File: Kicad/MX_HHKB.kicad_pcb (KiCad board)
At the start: 2 copper layers, 285.8 x 95.2 mm, 143 parts, among them J1 USB_mini_micro_B, K1 Esc, K10 9, K11 0, K12 -, K13 =, K14 Tab, K15 Q, K16 W, K17 E, K18 R, K19 T, K2 1, K20 Y, K21 U, K22 I, K23 O, K24 P, K25 [, K26 ], K27 Ctrl, K28 A, K29 S, K3 2, K30 D, K31 F, K32 G, K33 H, K34 J, K35 K, K36 L, K37 ;, K38 ', K39 Enter, K4 3, K40 L_Shift, K41 Z, K42 X, K43 C, K44 V, K45 B, K46 N, K47 M, K48 ,, K49 ., K5 4, K50 /, K51 R_Shift, K52 Fn, K53 L_GUI, K54 L_ALT, K55 SPACE, K56 R_ALT, K57 R_GUI, K58 `, K59 \, K6 5, K60 BACKSPACE, K61 Ctrl, K7 6, K8 7, K9 8, SW1 SW_PUSH, U0 ATMEGA32U4, X1 XTAL_GND

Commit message: - Added darkou and open hardware logo - Updated col/row assignation (simplifying rooting)
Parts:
- added G***: LOGO, Footprint:OPEN-HARDWARE, B.Cu at (192.2, 181.2)
- added G***: LOGO, Footprint:darkou, B.Cu at (236.8, 182.0)
- added G***: LOGO, Footprint:darkou, F.Cu at (234.5, 181.8)
- moved D14 10.5 mm to (96.2, 132.8), turned to 180 degrees
- moved R1 5.00 mm to (92.2, 152.5)
- moved C8 4.45 mm to (92.8, 171.2), turned to 0 degrees
- moved X1 3.82 mm to (96.0, 184.8)
- moved D1 3.01 mm to (82.5, 115.0)
- moved R3 2.30 mm to (72.0, 120.2)
- moved Poker_side_edge_long 0.91 mm to (352.2, 153.8)
- moved Poker_side_edge_long 0.66 mm to (66.8, 153.8)
- moved C1 0.35 mm to (91.5, 189.0), turned to 225 degrees
- turned SW1 to 90 degrees
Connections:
- U0 pad 11: /Col3 -> /Col1
- U0 pad 21: /Row0 -> /Col9
- U0 pad 22: /Row2 -> /Col4
- U0 pad 25: /Row1 -> /Col5
- U0 pad 28: /Col4 -> /Row1
- U0 pad 29: /Col5 -> /Row2
- U0 pad 31: /Col8 -> /Row0
- U0 pad 32: /Col9 -> /Col8
- U0 pad 9: /Col1 -> /Col3
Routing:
- net /Row3: track 266.9 -> 285.9 mm, vias 3 -> 2
- net VCC: track 171.3 -> 153.5 mm, vias 4 -> 2
- net GND: track 248.2 -> 262.9 mm, vias 0 -> 2
- net /Row4: track 364.7 -> 350.2 mm, vias 3 -> 1
- net /Col4: track 192.8 -> 179.1 mm, vias 3 -> 2
- net /Row1: track 323.8 -> 311.6 mm, vias 1 -> 2
- net /Row2: track 371.4 -> 359.4 mm
- net Net-(R1-Pad2): track 60.6 -> 51.1 mm, vias 2 -> 5
- net /Col5: track 235.8 -> 227.3 mm, vias 4 -> 2
- net Net-(D14-Pad2): track 9.39 -> 15.6 mm
- net Net-(C8-Pad1): track 12.5 -> 6.63 mm
- net Net-(C1-Pad1): track 18.5 -> 13.8 mm
- net Net-(J1-Pad2): track 27.0 -> 31.7 mm
- net /Col8: track 301.6 -> 296.9 mm, vias 7 -> 3
- net /Col12: track 360.7 -> 356.1 mm
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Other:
- board text added: "DK60 rev.A"

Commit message: - Rerouting some wires - Added led on Esc and Caps locks switches
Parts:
- added LD0: ESC_LED, LEDs:LED_D3.0mm, F.Cu at (75.0, 111.8)
- added LD1: CAPS_LED, LEDs:LED_D3.0mm, F.Cu at (77.2, 149.8)
- added LD2: CAPS_LED, LEDs:LED_D3.0mm, F.Cu at (84.8, 149.8)
- added R5: R, Resistors_SMD:R_0805_HandSoldering, B.Cu at (76.2, 116.0)
- added R6: R, Resistors_SMD:R_0805_HandSoldering, B.Cu at (84.0, 157.0)
- X1: footprint Crystals:Crystal_SMD_SeikoEpson_TSX3225-4pin_3.2x2.5mm_HandSoldering -> Footprint:FA-238
- moved R3 52.0 mm to (106.8, 159.0), turned to 45 degrees
- moved R4 50.0 mm to (109.5, 161.0), turned to 225 degrees
- moved C2 11.1 mm to (92.2, 186.0)
- moved C1 10.8 mm to (99.8, 182.0), turned to 315 degrees
- moved C8 2.26 mm to (90.5, 171.0)
- moved D1 1.90 mm to (84.2, 115.8), turned to 180 degrees
- moved R2 1.77 mm to (77.8, 167.5), turned to 135 degrees
- moved D54 1.27 mm to (143.0, 184.5)
- moved X1 1.03 mm to (97.0, 185.0), turned to 315 degrees
- moved C6 1.00 mm to (77.8, 162.5)
- moved C7 1.00 mm to (71.8, 164.8)
- moved C4 0.79 mm to (77.5, 158.0), turned to 225 degrees
- moved D53 0.75 mm to (119.0, 185.0)
- moved C5 0.50 mm to (71.8, 161.0)
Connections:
- U0 pad 15: Net-(U0-Pad15) -> GND
- U0 pad 23: Net-(U0-Pad23) -> GND
- U0 pad 28: /Row1 -> /Row2
- U0 pad 29: /Row2 -> /Row1
- U0 pad 40: Net-(U0-Pad40) -> /CAPS_LED
- U0 pad 41: Net-(U0-Pad41) -> /ESC_LED
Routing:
- net /Row0: track 458.2 -> 656.6 mm, vias 4 -> 3
- net /Row1: track 311.6 -> 405.6 mm, vias 2 -> 3
- net /ESC_LED: track 0.00 -> 63.0 mm, vias 0 -> 2
- net Net-(J1-Pad3): track 31.7 -> 84.2 mm, vias 0 -> 2
- net Net-(J1-Pad2): track 31.7 -> 84.1 mm, vias 0 -> 2
- net /Row2: track 359.4 -> 397.1 mm, vias 1 -> 3
- net Net-(R3-Pad1): track 58.7 -> 28.6 mm
- net Net-(R1-Pad2): track 51.1 -> 75.5 mm, vias 5 -> 4
- net Net-(R4-Pad2): track 53.3 -> 29.7 mm, vias 0 -> 2
- net /CAPS_LED: track 0.00 -> 21.3 mm, vias 0 -> 2
- net /Row3: track 285.9 -> 266.9 mm
- net GND: track 262.9 -> 246.7 mm, vias 2 -> 9
- net Net-(D27-Pad2): track 34.6 -> 23.4 mm
- net Net-(LD1-Pad2): track 0.00 -> 9.56 mm
- net /Col0: track 83.9 -> 90.8 mm
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
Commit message: - Some routing updates
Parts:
- moved R2 3.05 mm to (76.0, 170.0), turned to 90 degrees
- moved R3 1.06 mm to (106.0, 158.2)
- moved R4 1.03 mm to (109.8, 162.0)
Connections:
- U0 pad 1: Net-(U0-Pad1) -> /CAPS_LED
- U0 pad 21: /Col9 -> /Col4
- U0 pad 22: /Col4 -> /Col5
- U0 pad 25: /Col5 -> /Row4
- U0 pad 27: /Row4 -> /Row2
- U0 pad 28: /Row2 -> /Row1
- U0 pad 29: /Row1 -> /Col6
- U0 pad 30: /Col6 -> /Row0
- U0 pad 31: /Row0 -> /Col8
- U0 pad 32: /Col8 -> /Col9
- U0 pad 40: /CAPS_LED -> Net-(U0-Pad40)
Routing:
- net /Row2: track 397.1 -> 491.6 mm, vias 3 -> 0
- net GND: track 246.7 -> 321.7 mm, vias 9 -> 4
- net /Row1: track 405.6 -> 455.3 mm, vias 3 -> 0
- net /Col9: track 331.7 -> 369.9 mm, vias 1 -> 0
- net /Row0: track 656.6 -> 680.9 mm, vias 3 -> 1
- net /ESC_LED: track 63.0 -> 74.6 mm, vias 2 -> 0
- net /Col2: track 142.9 -> 132.3 mm, vias 3 -> 1
- net Net-(R1-Pad2): track 75.5 -> 65.2 mm, vias 4 -> 2
- net /Col5: track 226.2 -> 218.1 mm
- net /CAPS_LED: track 21.3 -> 13.9 mm, vias 2 -> 0
- net /Col8: track 302.0 -> 307.3 mm
- net Net-(R4-Pad2): track 29.7 -> 34.9 mm, vias 2 -> 0
- net Net-(J1-Pad3): track 84.2 -> 88.8 mm
- net /Col0: track 90.8 -> 86.3 mm
- net Net-(R2-Pad1): track 14.3 -> 9.86 mm
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
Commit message: - Cleaning routing, again and again
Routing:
- net /Row0: track 680.9 -> 572.9 mm, vias 1 -> 2
- net GND: track 321.7 -> 293.3 mm, vias 4 -> 1
- net /Row2: track 491.6 -> 480.6 mm
- net /Col8: track 307.3 -> 314.3 mm
- net Net-(J1-Pad2): track 82.5 -> 87.6 mm, vias 2 -> 0
- net /ESC_LED: track 74.6 -> 77.1 mm
- net Net-(J1-Pad3): track 88.8 -> 89.9 mm, vias 2 -> 0
- net Net-(R1-Pad2): track 65.2 -> 66.3 mm
- net /Col3: track 143.6 -> 142.8 mm

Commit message: - Updated layout to allow choice in 3 combinations for bottom row
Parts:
- removed K61: Ctrl, Footprint:Mx_Alps_175_STEPPED
- added K271: Ctrl, Footprint:Mx_Alps_175_STEPPED, F.Cu at (78.6, 145.3)
- added K541: L_ALT, Footprint:Mx_Alps_125, F.Cu at (131.0, 183.4)
- added K551: SPACE, Footprint:Mx_Alps_600, F.Cu at (214.3, 183.4)
- added K552: SPACE, Footprint:Mx_Alps_700, F.Cu at (209.6, 183.4)
- added K561: R_ALT, Footprint:Mx_Alps_150, F.Cu at (276.2, 183.4)
- added K562: R_ALT, Footprint:Mx_Alps_125, F.Cu at (288.1, 183.4)
- added K571: R_GUI, Footprint:Mx_Alps_100, F.Cu at (300.0, 183.4)
- added K572: R_GUI, Footprint:Mx_Alps_100, F.Cu at (309.6, 183.4)
- moved D56 25.4 mm to (264.9, 186.3)
- moved D55 8.50 mm to (224.8, 186.0)
- moved D57 7.85 mm to (321.3, 182.2)
- moved G*** 6.39 mm to (239.8, 178.2)
- moved G*** 3.87 mm to (238.4, 178.5)
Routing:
- net Net-(D56-Pad2): track 8.10 -> 32.9 mm
- net Net-(D57-Pad2): track 8.36 -> 28.8 mm
- net /Col9: track 369.9 -> 388.0 mm
- net /Row2: track 480.6 -> 498.5 mm
- net /Col8: track 314.3 -> 331.6 mm
- net /Row1: track 455.7 -> 469.2 mm
- net /Col5: track 218.1 -> 231.5 mm
- net /Col6: track 253.7 -> 266.0 mm
- net Net-(D55-Pad2): track 7.92 -> 16.7 mm
- net (no net): track 3.30 -> 10.7 mm
- net /Row0: track 572.9 -> 577.4 mm
- net Net-(D54-Pad2): track 7.97 -> 10.4 mm
- net /Col2: track 132.3 -> 134.7 mm
- net /Row4: track 348.3 -> 350.0 mm
- net /Col4: track 177.1 -> 178.4 mm
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
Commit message: - Updated bottom row
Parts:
- moved C1 4.31 mm to (96.3, 179.3), turned to 180 degrees
- moved X1 1.47 mm to (95.5, 185.2)
- moved C2 1.07 mm to (91.3, 185.6)
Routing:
- net Net-(D53-Pad2): track 7.99 -> 31.5 mm
- net /Col1: track 109.6 -> 118.7 mm
- net Net-(C2-Pad1): track 13.2 -> 11.6 mm
- net GND: track 293.3 -> 292.3 mm
- net /Col5: track 231.5 -> 232.1 mm

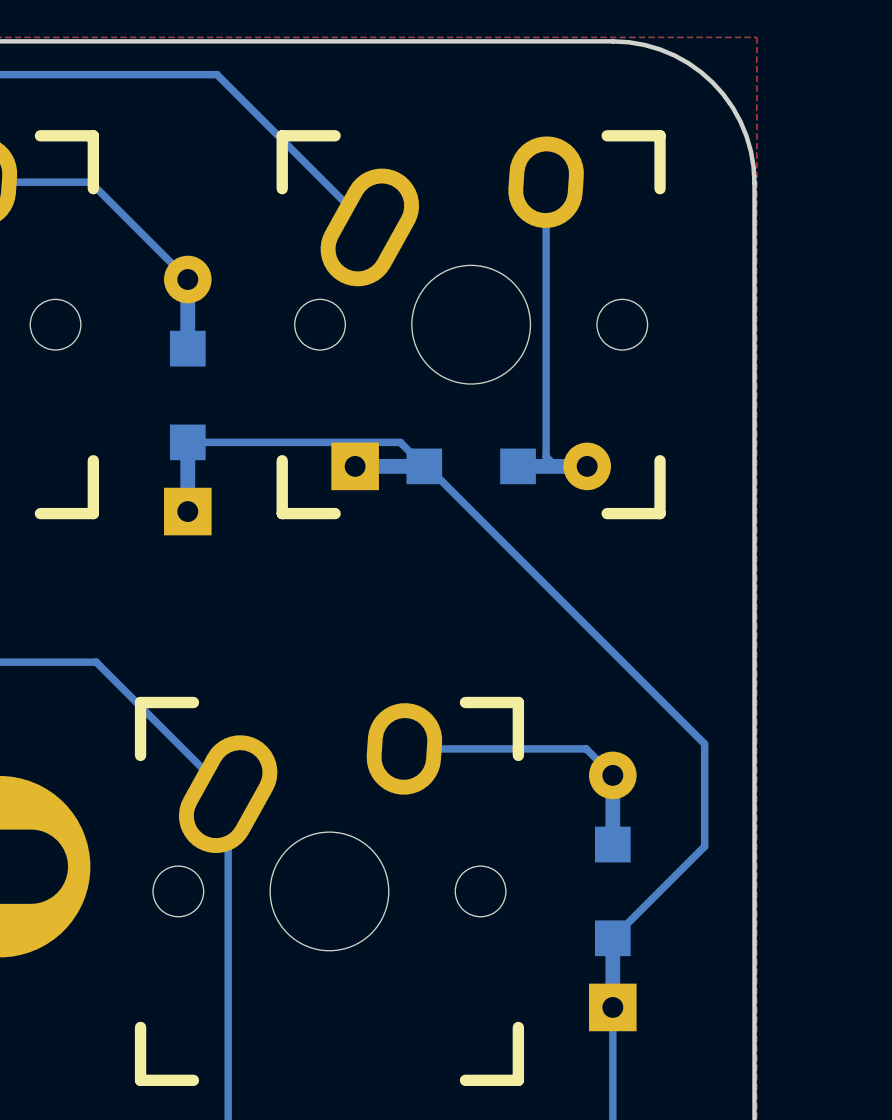
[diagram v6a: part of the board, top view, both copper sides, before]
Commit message: - Updated switches label (K00 to K4C) - Fixed footprint - Updated gerber files
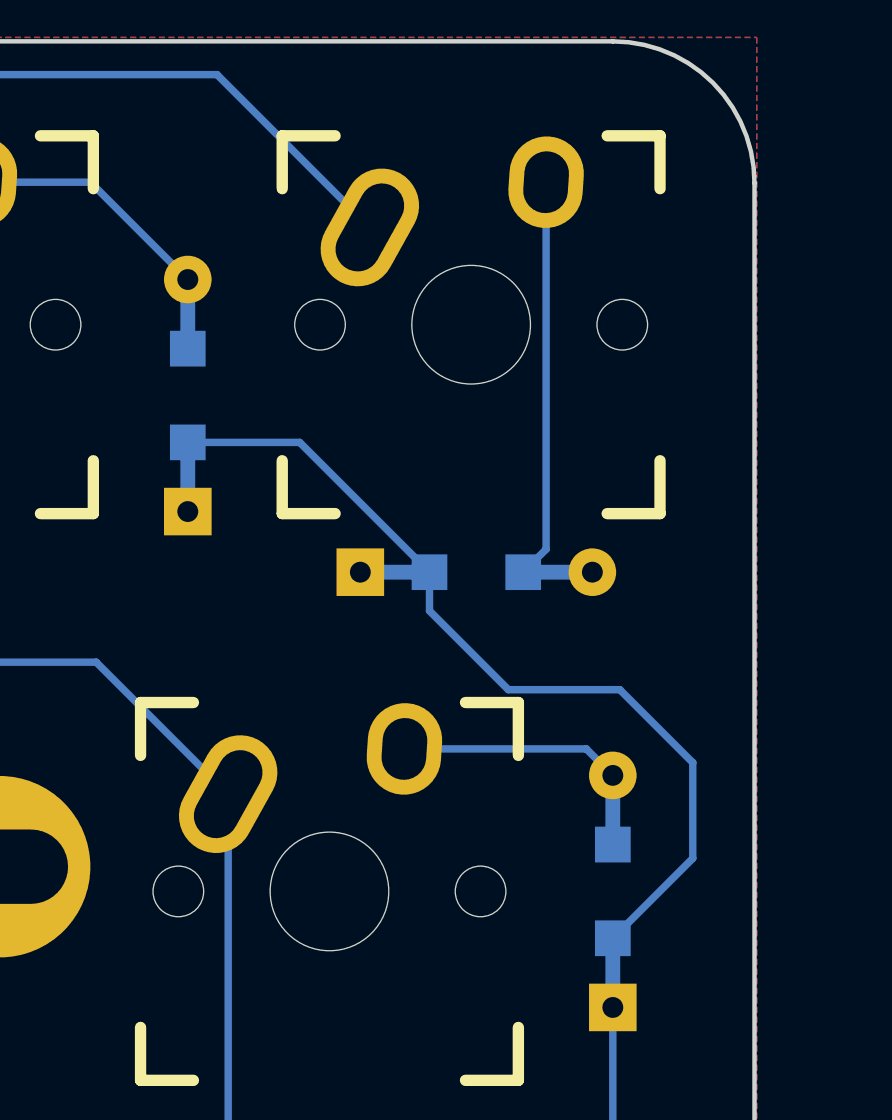
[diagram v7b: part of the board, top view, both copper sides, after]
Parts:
- removed K271: Ctrl, Footprint:Mx_Alps_175_STEPPED
- removed K541: L_ALT, Footprint:Mx_Alps_125
- removed K551: SPACE, Footprint:Mx_Alps_600
- removed K552: SPACE, Footprint:Mx_Alps_700
- removed K561: R_ALT, Footprint:Mx_Alps_150
- removed K562: R_ALT, Footprint:Mx_Alps_125
- removed K571, K572: R_GUI, Footprint:Mx_Alps_100
- added K61: Ctrl, Footprint:Mx_Alps_175_STEPPED, F.Cu at (78.6, 145.3)
- added K62: L_ALT, Footprint:Mx_Alps_125, F.Cu at (131.0, 183.4)
- added K63: SPACE, Footprint:Mx_Alps_700, F.Cu at (209.6, 183.4)
- added K64: SPACE, Footprint:Mx_Alps_600, F.Cu at (214.3, 183.4)
- added K65: R_ALT, Footprint:Mx_Alps_125, F.Cu at (288.1, 183.4)
- added K66: R_ALT, Footprint:Mx_Alps_150, F.Cu at (276.2, 183.4)
- added K67: R_GUI, Footprint:Mx_Alps_100, F.Cu at (309.6, 183.4)
- added K68: R_GUI, Footprint:Mx_Alps_100, F.Cu at (300.0, 183.4)
- K1: value Esc -> K00; footprint Fooprints:Mx_Alps_100 -> Footprint:Mx_Alps_100
- K10: value 9 -> K09; footprint Fooprints:Mx_Alps_100 -> Footprint:Mx_Alps_100
- K11: value 0 -> K0A; footprint Fooprints:Mx_Alps_100 -> Footprint:Mx_Alps_100
- K12: value - -> K0B; footprint Fooprints:Mx_Alps_100 -> Footprint:Mx_Alps_100
- K13: value = -> K0C; footprint Fooprints:Mx_Alps_100 -> Footprint:Mx_Alps_100
- K14: value Tab -> K10; footprint Fooprints:Mx_Alps_150 -> Footprint:Mx_Alps_150
- K15: value Q -> K11; footprint Fooprints:Mx_Alps_100 -> Footprint:Mx_Alps_100
- K16: value W -> K12; footprint Fooprints:Mx_Alps_100 -> Footprint:Mx_Alps_100
- K17: value E -> K13; footprint Fooprints:Mx_Alps_100 -> Footprint:Mx_Alps_100
- K18: value R -> K14; footprint Fooprints:Mx_Alps_100 -> Footprint:Mx_Alps_100
- K19: value T -> K15; footprint Fooprints:Mx_Alps_100 -> Footprint:Mx_Alps_100
- K2: value 1 -> K01; footprint Fooprints:Mx_Alps_100 -> Footprint:Mx_Alps_100
- K20: value Y -> K16; footprint Fooprints:Mx_Alps_100 -> Footprint:Mx_Alps_100
- K21: value U -> K17; footprint Fooprints:Mx_Alps_100 -> Footprint:Mx_Alps_100
- K22: value I -> K18; footprint Fooprints:Mx_Alps_100 -> Footprint:Mx_Alps_100
- K23: value O -> K19; footprint Fooprints:Mx_Alps_100 -> Footprint:Mx_Alps_100
- K24: value P -> K1A; footprint Fooprints:Mx_Alps_100 -> Footprint:Mx_Alps_100
- K25: value [ -> K1B; footprint Fooprints:Mx_Alps_100 -> Footprint:Mx_Alps_100
- K26: value ] -> K1C; footprint Fooprints:Mx_Alps_100 -> Footprint:Mx_Alps_100
- K27: value Ctrl -> K20; footprint Fooprints:Mx_Alps_175 -> Footprint:Mx_Alps_175
- K28: value A -> K21; footprint Fooprints:Mx_Alps_100 -> Footprint:Mx_Alps_100
- K29: value S -> K22; footprint Fooprints:Mx_Alps_100 -> Footprint:Mx_Alps_100
- K3: value 2 -> K02; footprint Fooprints:Mx_Alps_100 -> Footprint:Mx_Alps_100
- K30: value D -> K23; footprint Fooprints:Mx_Alps_100 -> Footprint:Mx_Alps_100
- K31: value F -> K24; footprint Fooprints:Mx_Alps_100 -> Footprint:Mx_Alps_100
- K32: value G -> K25; footprint Fooprints:Mx_Alps_100 -> Footprint:Mx_Alps_100
- K33: value H -> K26; footprint Fooprints:Mx_Alps_100 -> Footprint:Mx_Alps_100
- K34: value J -> K27; footprint Fooprints:Mx_Alps_100 -> Footprint:Mx_Alps_100
- K35: value K -> K28; footprint Fooprints:Mx_Alps_100 -> Footprint:Mx_Alps_100
- K36: value L -> K29; footprint Fooprints:Mx_Alps_100 -> Footprint:Mx_Alps_100
- K37: value ; -> K2A; footprint Fooprints:Mx_Alps_100 -> Footprint:Mx_Alps_100
- K38: value ' -> K2B; footprint Fooprints:Mx_Alps_100 -> Footprint:Mx_Alps_100
- K39: value Enter -> K2C
- K4: value 3 -> K03; footprint Fooprints:Mx_Alps_100 -> Footprint:Mx_Alps_100
- K40: value L_Shift -> K30; footprint Fooprints:Mx_Alps_175 -> Footprint:Mx_Alps_175
- K41: value Z -> K31; footprint Fooprints:Mx_Alps_100 -> Footprint:Mx_Alps_100
- K42: value X -> K32; footprint Fooprints:Mx_Alps_100 -> Footprint:Mx_Alps_100
- K43: value C -> K33; footprint Fooprints:Mx_Alps_100 -> Footprint:Mx_Alps_100
- K44: value V -> K34; footprint Fooprints:Mx_Alps_100 -> Footprint:Mx_Alps_100
- K45: value B -> K35; footprint Fooprints:Mx_Alps_100 -> Footprint:Mx_Alps_100
- K46: value N -> K36; footprint Fooprints:Mx_Alps_100 -> Footprint:Mx_Alps_100
- K47: value M -> K37; footprint Fooprints:Mx_Alps_100 -> Footprint:Mx_Alps_100
- K48: value , -> K38; footprint Fooprints:Mx_Alps_100 -> Footprint:Mx_Alps_100
- K49: value . -> K39; footprint Fooprints:Mx_Alps_100 -> Footprint:Mx_Alps_100
- K5: value 4 -> K04; footprint Fooprints:Mx_Alps_100 -> Footprint:Mx_Alps_100
- K50: value / -> K3A; footprint Fooprints:Mx_Alps_100 -> Footprint:Mx_Alps_100
- K51: value R_Shift -> K3B; footprint Fooprints:Mx_Alps_125 -> Footprint:Mx_Alps_125
- K52: value Fn -> K3C; footprint Fooprints:Mx_Alps_100 -> Footprint:Mx_Alps_100
- K53: value L_GUI -> K41; footprint Fooprints:Mx_Alps_100 -> Footprint:Mx_Alps_100
- K54: value L_ALT -> K42; footprint Fooprints:Mx_Alps_150 -> Footprint:Mx_Alps_150
- K55: value SPACE -> K45
- K56: value R_ALT -> K48; footprint Fooprints:Mx_Alps_150 -> Footprint:Mx_Alps_150
- K57: value R_GUI -> K49; footprint Fooprints:Mx_Alps_100 -> Footprint:Mx_Alps_100
- K58: value ` -> K4A; footprint Fooprints:Mx_Alps_100 -> Footprint:Mx_Alps_100
- K59: value \ -> K4B; footprint Fooprints:Mx_Alps_100 -> Footprint:Mx_Alps_100
- K6: value 5 -> K05; footprint Fooprints:Mx_Alps_100 -> Footprint:Mx_Alps_100
- K60: value BACKSPACE -> K4C; footprint Fooprints:Mx_Alps_150 -> Footprint:Mx_Alps_150
- K7: value 6 -> K06; footprint Fooprints:Mx_Alps_100 -> Footprint:Mx_Alps_100
- K8: value 7 -> K07; footprint Fooprints:Mx_Alps_100 -> Footprint:Mx_Alps_100
- K9: value 8 -> K08; footprint Fooprints:Mx_Alps_100 -> Footprint:Mx_Alps_100
- moved D58 3.56 mm to (343.1, 115.5)
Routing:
- net Net-(D58-Pad2): track 9.80 -> 13.4 mm

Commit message: - Replaced all Diodes with SMD
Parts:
- D1, D10, D11, D12, D13, D14, D15, D16, D17, D18, D19, D2, D20, D21, D22, D23, D24, D25, D26, D27, D28, D29, D3, D30, D31, D32, D33, D34, D35, D36, D37, D38, D39, D4, D40, D41, D42, D43, D44, D45, D46, D47, D48, D49, D5, D50, D51, D52, D53, D54, D55, D56, D57, D58, D59, D6, D60, D7, D8, D9: footprint Fooprints:D_SOD123_axial -> Footprint:D_SOD123
- J1: footprint Fooprints:USB_miniB_hirose_5S8 -> Footprint:USB_miniB_hirose_5S8
- moved D26 1.94 mm to (321.5, 130.5)
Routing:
- net /Row0: track 577.4 -> 603.9 mm, vias 2 -> 12
- net Net-(D53-Pad2): track 31.5 -> 10.2 mm
- net Net-(J1-Pad2): track 87.6 -> 68.6 mm
- net Net-(J1-Pad3): track 89.9 -> 73.3 mm
- net /Row2: track 498.5 -> 483.1 mm, vias 0 -> 4
- net (no net): track 10.4 -> 0.00 mm
- net /Col5: track 232.1 -> 242.0 mm
- net /Col6: track 266.0 -> 261.4 mm
- net Net-(D26-Pad2): track 5.98 -> 9.35 mm
- net /Col8: track 331.6 -> 328.3 mm, vias 0 -> 1
- net /Row1: track 469.2 -> 472.6 mm, vias 0 -> 2
- net /Row4: track 349.9 -> 352.8 mm, vias 0 -> 3
- net Net-(D29-Pad2): track 8.36 -> 10.8 mm
- net Net-(D41-Pad2): track 8.36 -> 10.8 mm
- net Net-(D34-Pad2): track 8.36 -> 10.8 mm
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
